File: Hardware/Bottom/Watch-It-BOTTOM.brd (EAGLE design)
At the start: 33 x 33 mm, 31 parts, among them U1 AD5242-SO16

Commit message: routed bottom board 6/10
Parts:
- moved C22 37.1 mm to (11.7, 27.6), turned to 90 degrees
- moved OP4 34.7 mm to (11.0, 31.4), turned to 180 degrees
- moved R19 23.4 mm to (14.4, 29.0)
- moved R18 22.3 mm to (33.1, 31.4), turned to 90 degrees
- moved R17 18.8 mm to (30.3, 31.4)
- moved R23 18.6 mm to (33.0, 28.3), turned to 270 degrees
- moved C10 13.0 mm to (13.4, 31.4)
- moved C21 11.9 mm to (32.9, 17.9)
- moved C19 11.7 mm to (31.5, 25.6), turned to 90 degrees
- moved R24 11.6 mm to (32.8, 20.6), turned to 90 degrees
- moved C20 11.5 mm to (33.0, 24.3), turned to 270 degrees
- moved C18 9.22 mm to (20.4, 8.10)
- moved R22 9.08 mm to (29.8, 26.1), turned to 270 degrees
- moved R21 7.32 mm to (30.4, 29.0), turned to 180 degrees
- moved R20 6.58 mm to (31.2, 33.9)
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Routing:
- net GND: track 0.00 -> 38.1 mm, vias 0 -> 10
- net 3.3V: track 0.00 -> 34.1 mm, vias 0 -> 5
- net TIA: track 0.00 -> 32.9 mm, vias 0 -> 2
- net N$15: track 0.00 -> 32.6 mm, vias 0 -> 2
- net PPG: track 0.00 -> 32.0 mm, vias 0 -> 2
- net PD.C: track 0.00 -> 32.0 mm
- net G.W2: track 0.00 -> 31.5 mm, vias 0 -> 2
- net VREF: track 0.00 -> 18.1 mm
- net SDA: track 0.00 -> 16.7 mm, vias 0 -> 2
- net SCL: track 0.00 -> 15.1 mm, vias 0 -> 2
- net N$17: track 0.00 -> 9.77 mm
- net N$13: track 0.00 -> 9.20 mm
- net N$16: track 0.00 -> 8.17 mm
- net N$9: track 0.00 -> 6.26 mm
- net N$18: track 0.00 -> 6.24 mm
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
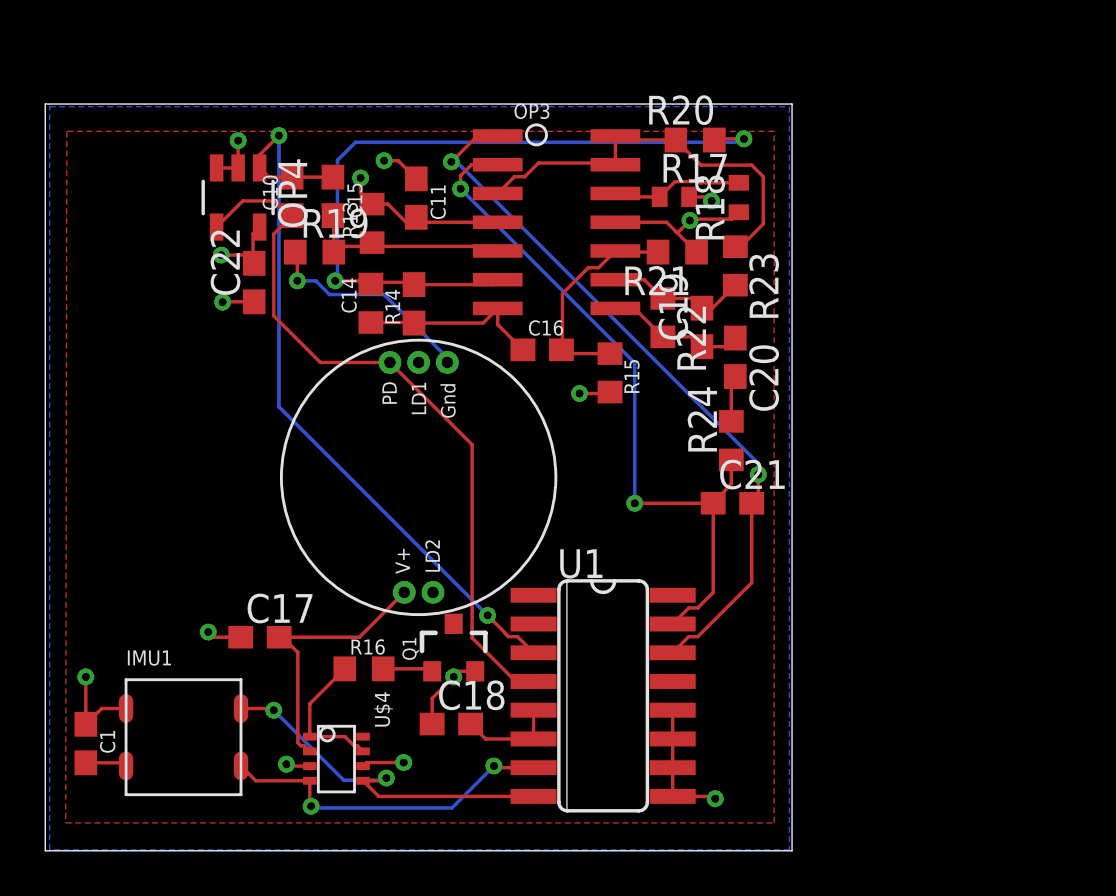
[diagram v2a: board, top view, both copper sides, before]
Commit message: rotated and added pins
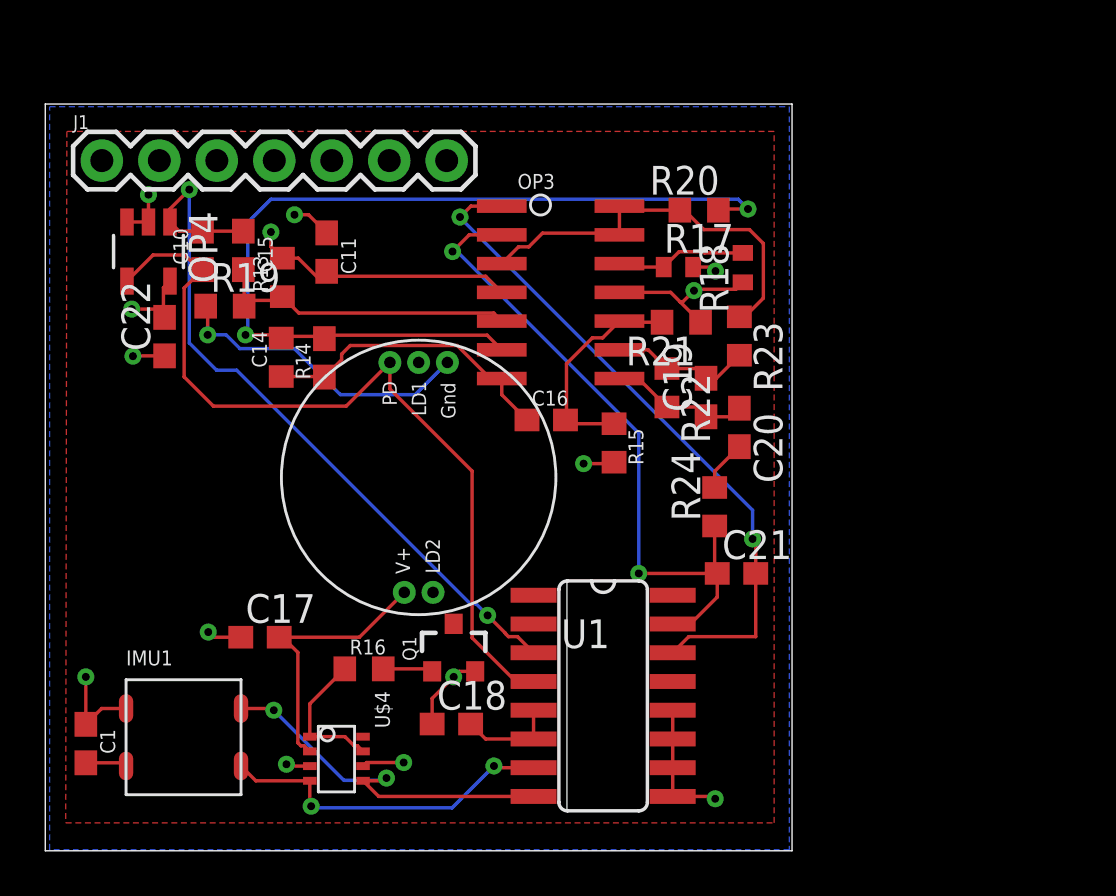
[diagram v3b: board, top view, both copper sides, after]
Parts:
- added J1: (no value), LinnesLab-Connectors:1X07
- moved C14 4.63 mm to (14.8, 24.3)
- moved C11 4.63 mm to (14.9, 29.0)
- moved C15 4.63 mm to (11.3, 29.0)
- moved C22 4.63 mm to (7.77, 25.2)
- moved OP4 4.63 mm to (7.06, 29.0)
- moved R13 4.63 mm to (13.0, 27.8)
- moved R19 4.63 mm to (10.4, 26.6)
- moved C10 4.63 mm to (9.45, 29.0)
- moved R14 4.63 mm to (12.9, 24.3)
- moved C16 3.10 mm to (24.6, 21.5)
- moved C20 3.10 mm to (33.2, 21.2)
- moved C21 3.10 mm to (33.0, 14.8)
- moved OP3 3.10 mm to (25.3, 27.2)
- moved R15 3.10 mm to (27.6, 20.5)
- moved R17 3.10 mm to (30.5, 28.3)
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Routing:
- net N$15: track 32.6 -> 40.9 mm
- net N$16: track 8.17 -> 13.4 mm
- net PD.C: track 32.0 -> 36.7 mm
- net 3.3V: track 34.1 -> 38.5 mm
- net N$13: track 9.20 -> 13.6 mm
- net GND: track 38.1 -> 42.2 mm
- net G.W2: track 31.5 -> 29.4 mm
- net PPG: track 32.0 -> 30.0 mm

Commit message: pushing old edits
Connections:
- removed net LED.CTRL: U$4.8
- removed net PPG: C21.2, OP3.1, U1.14
- removed net TIA: C10.2, C15.1, OP4.1, U1.3
- new net A6/TIA: C10.2, C15.1, J1.5, OP4.1, U1.3
- new net A7/PPG: C21.2, J1.7, OP3.1, U1.14
- new net D29/LED.CTRL: J1.6, U$4.8
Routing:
- net TIA: track 32.9 -> 0.00 mm, vias 2 -> 0
- net A6/TIA: track 0.00 -> 32.9 mm, vias 0 -> 2
- net PPG: track 30.0 -> 0.00 mm, vias 2 -> 0
- net A7/PPG: track 0.00 -> 30.0 mm, vias 0 -> 2
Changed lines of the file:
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@@
 <wire x1="14.1906" y1="4.5292" x2="14.1906" y2="5.5938" width="0.1524" layer="1"/>
 </signal>
-<signal name="TIA">
+<signal name="A6/TIA">
 <contactref element="C10" pad="2"/>
 <contactref element="U1" pad="3"/>
@@
 <wire x1="8.8646" y1="31.7182" x2="8.0112" y2="30.8648" width="0.1524" layer="1"/>
 <wire x1="8.0112" y1="30.8648" x2="8.0112" y2="30.2874" width="0.1524" layer="1"/>
+<contactref element="J1" pad="5"/>
+<wire x1="11.2522" y1="29.8822" x2="15.16" y2="33" width="0" layer="19" extent="1-1"/>
 </signal>
 <signal name="PD.C">
@@
 <wire x1="16.1487125" y1="7.1402" x2="15.7451125" y2="7.5438" width="0.1524" layer="1"/>
 </signal>
-<signal name="LED.CTRL">
+<signal name="D29/LED.CTRL">
 <contactref element="U$4" pad="8"/>
+<contactref element="J1" pad="6"/>
+<wire x1="16.5434" y1="7.5438" x2="17.7" y2="33" width="0" layer="19" extent="1-1"/>
 </signal>
 <signal name="N$10">
@@
 <contactref element="U1" pad="1"/>
 </signal>
-<signal name="PPG">
+<signal name="A7/PPG">
 <contactref element="U1" pad="14"/>
 <contactref element="C21" pad="2"/>
@@
 <wire x1="33.7566" y1="16.2814" x2="33.8954" y2="16.1426" width="0.1524" layer="1"/>
 <wire x1="33.8954" y1="16.1426" x2="33.8954" y2="14.7574" width="0.1524" layer="1"/>
+<contactref element="J1" pad="7"/>
+<wire x1="20.828" y1="30.5054" x2="20.24" y2="33" width="0" layer="19" extent="1-1"/>
 </signal>
 <signal name="N$13">

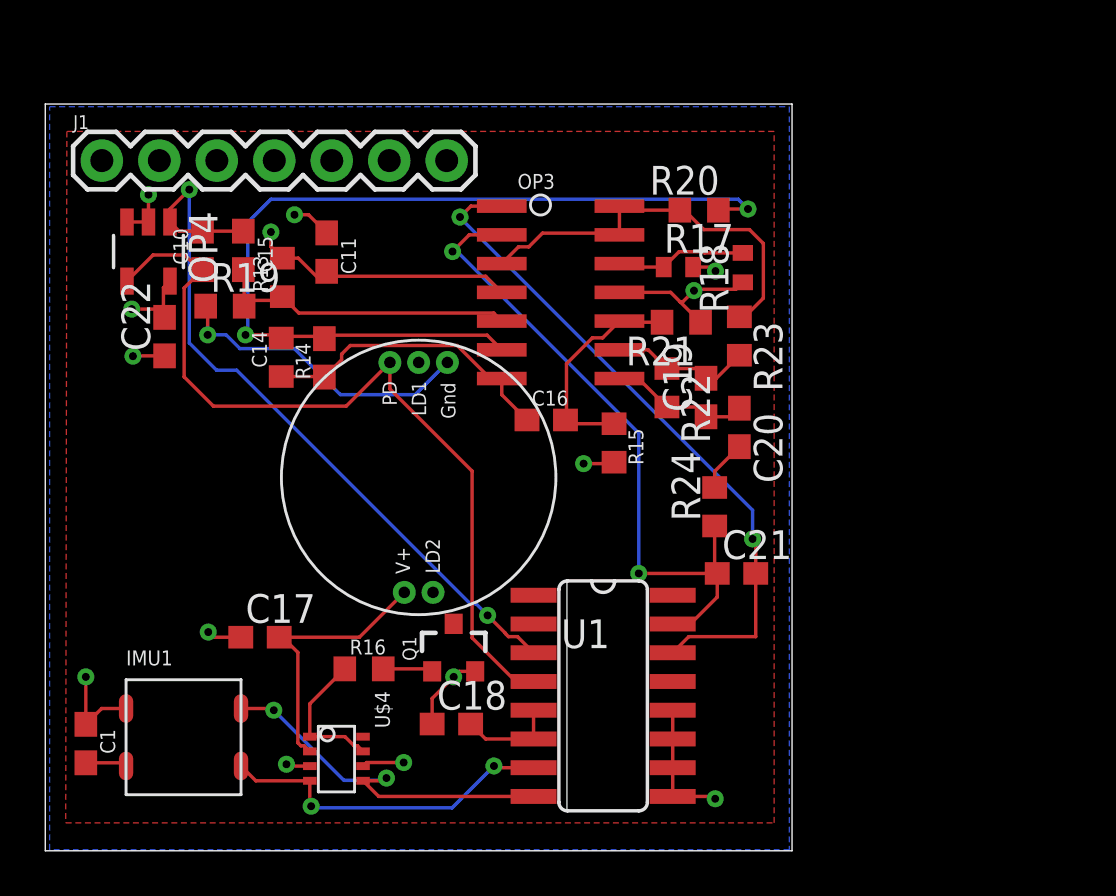
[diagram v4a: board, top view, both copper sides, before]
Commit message: fixed polygon and wire stubs
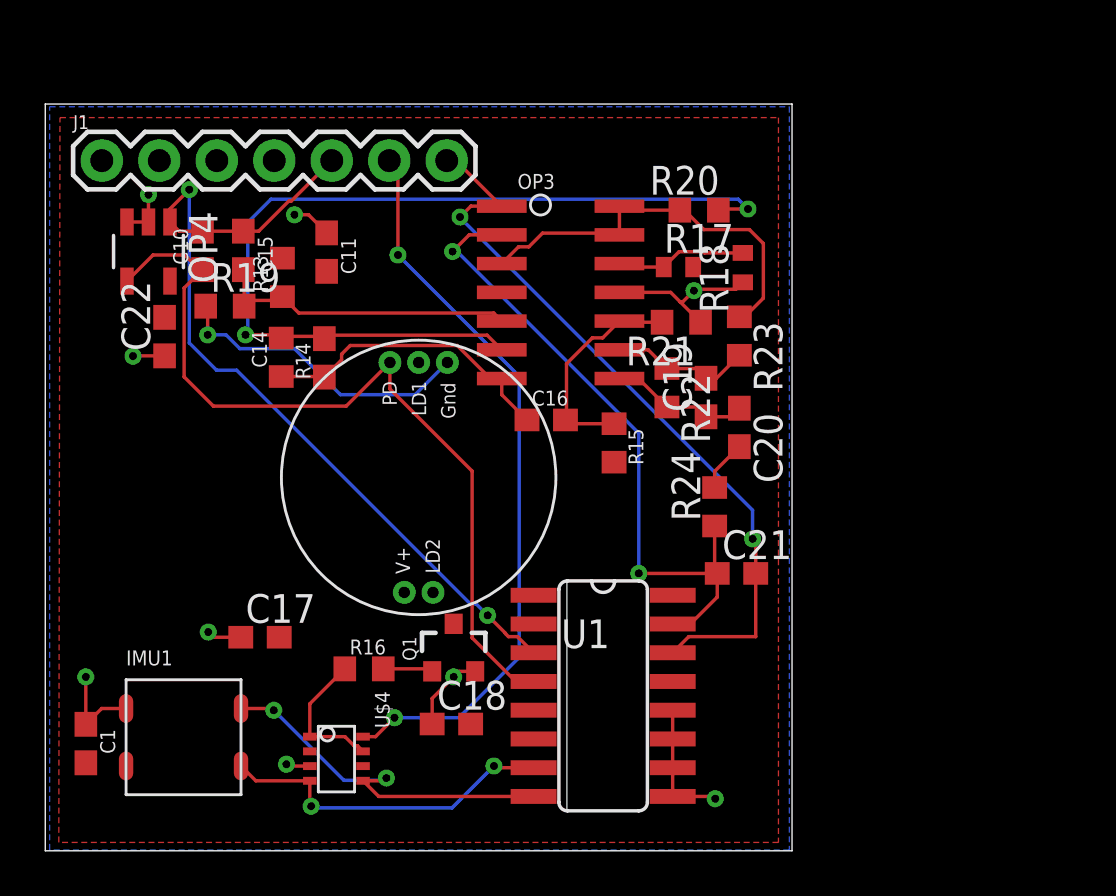
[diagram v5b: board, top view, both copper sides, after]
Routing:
- net 3.3V: track 38.5 -> 1.03 mm, vias 5 -> 0
- net D29/LED.CTRL: track 0.00 -> 32.9 mm, vias 0 -> 2
- net A6/TIA: track 32.9 -> 38.1 mm
- net A7/PPG: track 30.0 -> 33.2 mm
- added copper zone on layer 1, net 3.3V
- removed copper zone on layer 1, net 9V
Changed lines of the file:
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@@
 <contactref element="IMU1" pad="2"/>
 <contactref element="C1" pad="2"/>
-<wire x1="4.2926" y1="6.389" x2="6.0706" y2="6.389" width="0.1524" layer="1"/>
 <wire x1="6.0706" y1="6.389" x2="6.0706" y2="6.2484" width="0.1524" layer="1"/>
-<wire x1="13.662" y1="7.2741125" x2="13.7959125" y2="7.1402" width="0.1524" layer="1"/>
-<wire x1="13.7959125" y1="7.1402" x2="13.9442" y2="7.1402" width="0.1524" layer="1"/>
-<wire x1="13.9442" y1="7.1402" x2="14.1906" y2="6.8938" width="0.1524" layer="1"/>
-<wire x1="13.662" y1="11.2672" x2="13.662" y2="7.2741125" width="0.1524" layer="1"/>
-<wire x1="16.5434" y1="6.2438" x2="16.7004" y2="6.4008" width="0.1524" layer="1"/>
-<wire x1="16.7004" y1="6.4008" x2="18.3388" y2="6.4008" width="0.1524" layer="1"/>
-<via x="18.3388" y="6.4008" extent="1-16" drill="0.35"/>
-<wire x1="31.13" y1="28.2956" x2="31.94181875" y2="28.2956" width="0.1524" layer="1"/>
-<wire x1="31.94181875" y1="28.2956" x2="32.11961875" y2="28.1178" width="0.1524" layer="1"/>
-<via x="32.11961875" y="28.1178" extent="1-16" drill="0.35"/>
-<wire x1="12.9794" y1="28.6884" x2="12.4714" y2="29.1964" width="0.1524" layer="1"/>
-<wire x1="12.4714" y1="29.845" x2="12.4714" y2="29.1964" width="0.1524" layer="1"/>
-<via x="12.4714" y="29.845" extent="1-16" drill="0.35"/>
-<wire x1="7.7216" y1="27.3858" x2="8.0112" y2="27.6754" width="0.1524" layer="1"/>
 <wire x1="14.9352" y1="28.106" x2="14.911909375" y2="28.278765625" width="0.1524" layer="1"/>
-<via x="6.321875" y="26.438675" extent="1-16" drill="0.35"/>
-<wire x1="18.365" y1="13.92" x2="16.383" y2="11.938" width="0.1524" layer="1"/>
 <wire x1="12.8388" y1="11.938" x2="12.9912" y2="11.938" width="0.1524" layer="1"/>
-<wire x1="12.9912" y1="11.938" x2="13.662" y2="11.2672" width="0.1524" layer="1"/>
-<wire x1="12.8388" y1="11.938" x2="16.383" y2="11.938" width="0.1524" layer="1"/>
-<wire x1="21.297" y1="8.1026" x2="21.9574" y2="7.4422" width="0.1524" layer="1"/>
-<wire x1="21.9574" y1="7.4422" x2="24.0792" y2="7.4422" width="0.1524" layer="1"/>
-<wire x1="24.0792" y1="7.4422" x2="24.0792" y2="8.7122" width="0.1524" layer="1"/>
-<wire x1="27.6352" y1="19.6732" x2="27.5708" y2="19.6088" width="0.1524" layer="1"/>
-<wire x1="27.5708" y1="19.6088" x2="26.289" y2="19.6088" width="0.1524" layer="1"/>
-<via x="26.289" y="19.6088" extent="1-16" drill="0.35"/>
-<wire x1="7.7724" y1="26.0722" x2="7.7216" y2="26.123" width="0.1524" layer="1"/>
-<wire x1="7.7216" y1="26.123" x2="7.7216" y2="27.3858" width="0.1524" layer="1"/>
-<wire x1="7.7724" y1="26.0722" x2="7.405925" y2="26.438675" width="0.1524" layer="1"/>
-<wire x1="7.405925" y1="26.438675" x2="6.321875" y2="26.438675" width="0.1524" layer="1"/>
-<wire x1="22.673" y1="27.178" x2="21.9618" y2="27.8892" width="0.1524" layer="1"/>
-<wire x1="21.9618" y1="27.8892" x2="15.336246875" y2="27.8892" width="0.1524" layer="1"/>
 <wire x1="15.13193125" y1="28.093515625" x2="15.336246875" y2="27.8892" width="0.1524" layer="1"/>
-<wire x1="14.6906875" y1="27.678615625" x2="14.9493125" y2="27.678615625" width="0.1524" layer="1"/>
 <wire x1="14.9493125" y1="27.678615625" x2="15.142759375" y2="27.8720625" width="0.1524" layer="1"/>
-<wire x1="15.142759375" y1="27.8720625" x2="15.142759375" y2="28.264115625" width="0.1524" layer="1"/>
-<wire x1="12.9794" y1="28.6884" x2="13.680903125" y2="28.6884" width="0.1524" layer="1"/>
-<wire x1="13.680903125" y1="28.6884" x2="14.6906875" y2="27.678615625" width="0.1524" layer="1"/>
-<wire x1="22.673" y1="27.178" x2="31.13" y2="28.2956" width="0" layer="19" extent="1-1"/>
-<wire x1="15.142759375" y1="28.264115625" x2="15.13193125" y2="28.093515625" width="0" layer="19" extent="1-1"/>
-<wire x1="14.9352" y1="28.106" x2="15.13193125" y2="28.093515625" width="0" layer="19" extent="1-1"/>
-<wire x1="8.0112" y1="27.6754" x2="12.4714" y2="29.845" width="0" layer="19" extent="1-1"/>
-<wire x1="26.289" y1="19.6088" x2="22.673" y2="27.178" width="0" layer="19" extent="1-1"/>
-<wire x1="18.365" y1="13.92" x2="26.289" y2="19.6088" width="0" layer="19" extent="1-1"/>
-<wire x1="16.5434" y1="6.2438" x2="14.1906" y2="6.8938" width="0" layer="19" extent="1-1"/>
-<wire x1="21.297" y1="8.1026" x2="18.3388" y2="6.4008" width="0" layer="19" extent="1-1"/>
-<wire x1="6.0706" y1="6.2484" x2="14.1906" y2="6.8938" width="0" layer="19" extent="1-1"/>
+<polygon width="0.1524" layer="1">
+<vertex x="3.1496" y="34.8996"/>
+<vertex x="34.8996" y="34.8996"/>
+<vertex x="34.8996" y="2.8702"/>
+<vertex x="3.0988" y="2.8702"/>
+</polygon>
 </signal>
 <signal name="SDA">
@@
 <contactref element="C15" pad="1"/>
 <contactref element="OP4" pad="1"/>
-<wire x1="11.2522" y1="29.8822" x2="9.4488" y2="29.8822" width="0.1524" layer="1"/>
+<wire x1="11.2522" y1="29.8822" x2="10.9982" y2="29.8822" width="0.1524" layer="1"/>
+<wire x1="10.9982" y1="29.8822" x2="9.4488" y2="29.8822" width="0.1524" layer="1"/>
 <wire x1="8.0112" y1="30.2874" x2="8.4164" y2="29.8822" width="0.1524" layer="1"/>
 <wire x1="8.4164" y1="29.8822" x2="9.4488" y2="29.8822" width="0.1524" layer="1"/>
@@
 <wire x1="8.0112" y1="30.8648" x2="8.0112" y2="30.2874" width="0.1524" layer="1"/>
 <contactref element="J1" pad="5"/>
-<wire x1="11.2522" y1="29.8822" x2="15.16" y2="33" width="0" layer="19" extent="1-1"/>
+<wire x1="15.16" y1="33" x2="13.3738" y2="31.2138" width="0.1524" layer="1"/>
+<wire x1="13.3738" y1="31.2138" x2="13.26145" y2="31.2138" width="0.1524" layer="1"/>
+<wire x1="11.92985" y1="29.8822" x2="11.2522" y2="29.8822" width="0.1524" layer="1"/>
+<wire x1="13.26145" y1="31.2138" x2="11.92985" y2="29.8822" width="0.1524" layer="1"/>
 </signal>
 <signal name="PD.C">
@@
 <contactref element="U$4" pad="8"/>
 <contactref element="J1" pad="6"/>
-<wire x1="16.5434" y1="7.5438" x2="17.7" y2="33" width="0" layer="19" extent="1-1"/>
+<wire x1="17.7" y1="33" x2="18.0848" y2="33" width="0.1524" layer="1"/>
+<wire x1="18.0848" y1="33" x2="18.0848" y2="28.829" width="0.1524" layer="1"/>
+<via x="18.0848" y="28.829" extent="1-16" drill="0.35"/>
+<wire x1="18.0848" y1="28.829" x2="23.4442" y2="23.4696" width="0.1524" layer="16"/>
+<wire x1="23.4442" y1="23.4696" x2="23.4442" y2="11.049" width="0.1524" layer="16"/>
+<wire x1="23.4442" y1="11.049" x2="20.7772" y2="8.382" width="0.1524" layer="16"/>
+<wire x1="20.7772" y1="8.382" x2="17.9324" y2="8.382" width="0.1524" layer="16"/>
+<via x="17.9324" y="8.382" extent="1-16" drill="0.35"/>
+<wire x1="17.9324" y1="8.382" x2="17.0942" y2="7.5438" width="0.1524" layer="1"/>
+<wire x1="17.0942" y1="7.5438" x2="16.5434" y2="7.5438" width="0.1524" layer="1"/>
 </signal>
 <signal name="N$10">
@@
 <wire x1="30.9372" y1="11.9634" x2="33.8954" y2="11.9634" width="0.1524" layer="1"/>
 <wire x1="33.8954" y1="11.9634" x2="33.8954" y2="14.7574" width="0.1524" layer="1"/>
-<wire x1="22.673" y1="30.988" x2="21.3106" y2="30.988" width="0.1524" layer="1"/>
+<wire x1="22.673" y1="30.988" x2="22.6568" y2="30.988" width="0.1524" layer="1"/>
+<wire x1="22.6568" y1="30.988" x2="21.3106" y2="30.988" width="0.1524" layer="1"/>
 <wire x1="21.3106" y1="30.988" x2="20.828" y2="30.5054" width="0.1524" layer="1"/>
 <via x="20.828" y="30.5054" extent="1-16" drill="0.35"/>
@@
 <wire x1="33.8954" y1="16.1426" x2="33.8954" y2="14.7574" width="0.1524" layer="1"/>
 <contactref element="J1" pad="7"/>
-<wire x1="20.828" y1="30.5054" x2="20.24" y2="33" width="0" layer="19" extent="1-1"/>
+<wire x1="20.24" y1="33" x2="20.6448" y2="33" width="0.1524" layer="1"/>
+<wire x1="20.6448" y1="33" x2="22.6568" y2="30.988" width="0.1524" layer="1"/>
 </signal>
 <signal name="N$13">
@@
 <wire x1="32.0802" y1="19.2668" x2="33.1724" y2="20.359" width="0.1524" layer="1"/>
 </signal>
-<signal name="9V">
-<polygon width="0.1524" layer="1">
-<vertex x="3.4036" y="3.7338"/>
-<vertex x="34.7091" y="3.7338"/>
-<vertex x="34.7091" y="34.29"/>
-<vertex x="3.454484375" y="34.29"/>
-</polygon>
-</signal>
 </signals>
